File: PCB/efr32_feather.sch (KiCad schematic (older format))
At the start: 38 parts, among them J1 Feather_1, J2 USB, J3 Battery, J4 Feather_2, J5 DEBUG, Q1 DMG2301L, SW1 RESET, U1 TPD2EUSB30, U2 AP2112K-3.3, U3 CP2102N-A01-GQFN24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

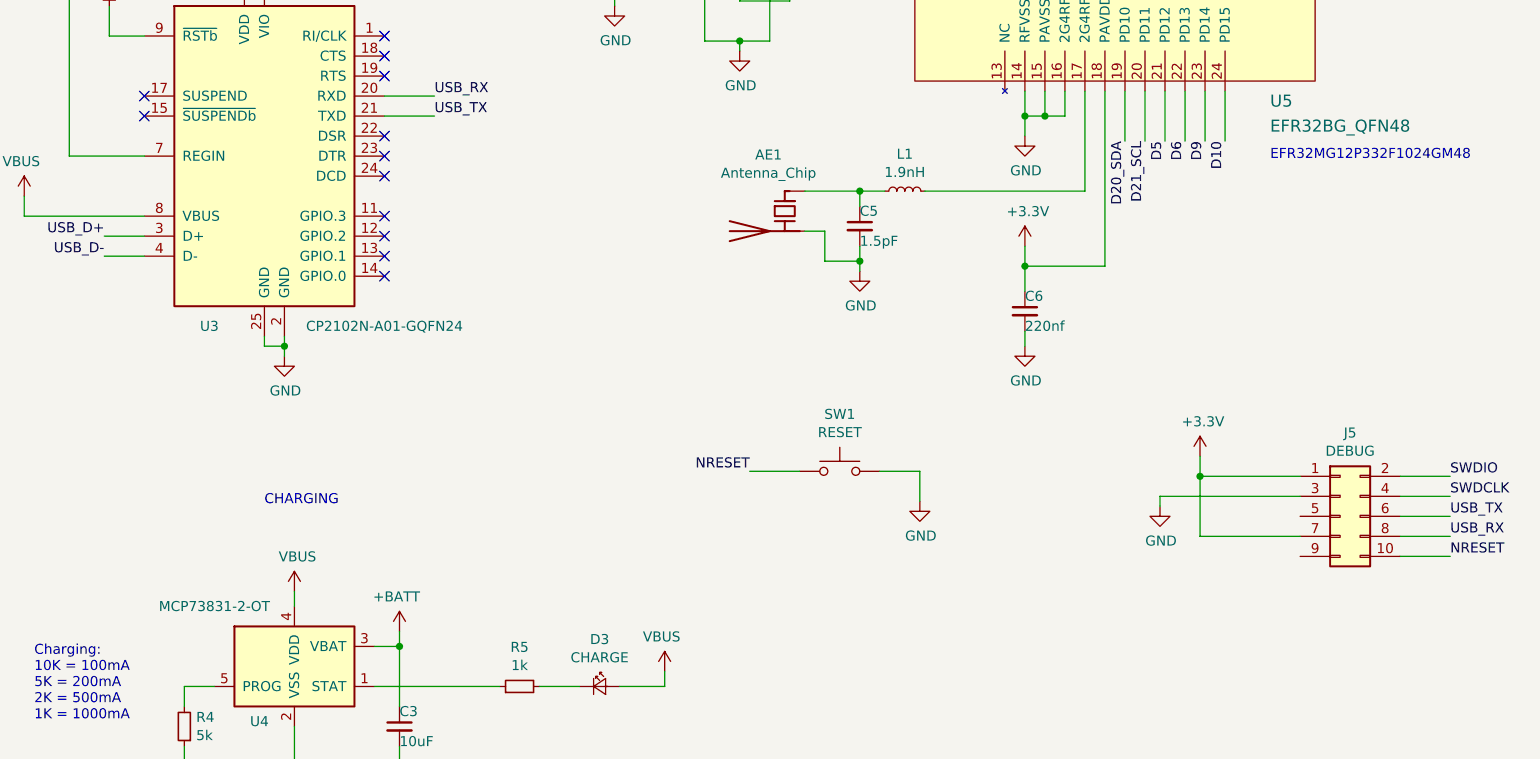
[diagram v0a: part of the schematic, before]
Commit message: Change debug connector
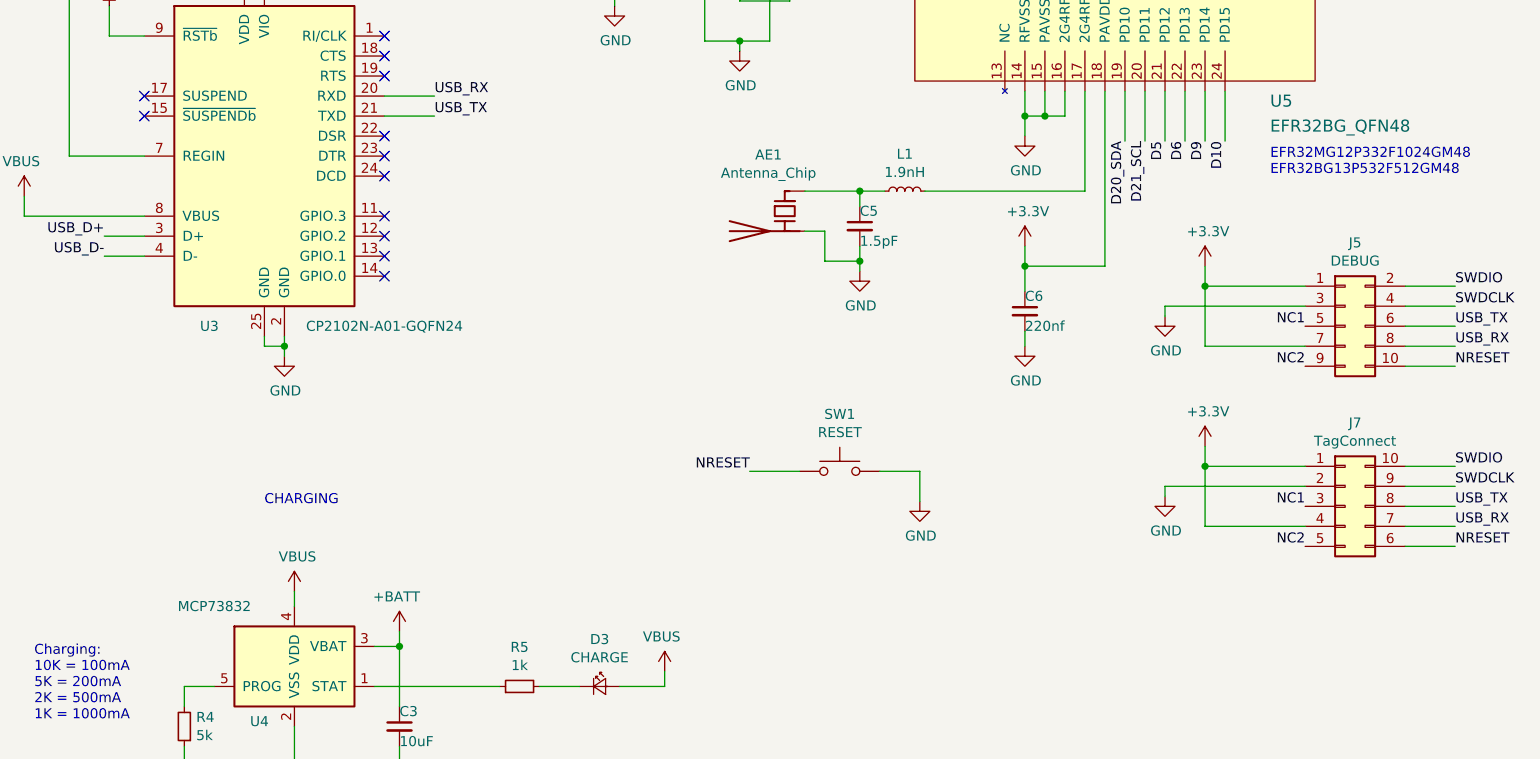
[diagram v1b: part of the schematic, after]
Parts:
- added J7: TagConnect, Connector:Tag-Connect_TC2050-IDC-NL_2x05_P1.27mm_Vertical, symbol Connector_Generic:Conn_02x05_Counter_Clockwise
- J5: footprint Connector_PinHeader_1.00mm:PinHeader_2x05_P1.00mm_Vertical_SMD -> Connector_PinHeader_1.27mm:PinHeader_2x05_P1.27mm_Vertical_SMD
- U4: value MCP73831-2-OT -> MCP73832
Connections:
- net +3V3: now also J7.1 (Pin_1), J7.4 (Pin_4)
- net GND: now also J7.2 (Pin_2)
- net NRESET: now also J7.6 (Pin_6)
- net SWDCLK: now also J7.9 (Pin_9)
- net SWDIO: now also J7.10 (Pin_10)
- net USB_RX: now also J7.7 (Pin_7)
- net USB_TX: now also J7.8 (Pin_8)
- net NC1: now reaches J5.5 (Pin_5)
- net NC1: now also J7.3 (Pin_3)
- net NC2: now reaches J5.9 (Pin_9)
- net NC2: now also J7.5 (Pin_5)
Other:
- note added: "EFR32MG12P332F1024GM48\nEFR32BG13P532F512GM48"
- note removed: "EFR32MG12P332F1024GM48"
- moved on the sheet: J5
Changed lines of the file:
@@
 Sheet 1 1
 Title "EFR32 Feather"
-Date "2019-06-07"
-Rev "0.2"
+Date "2019-06-20"
+Rev "0.3"
 Comp ""
 Comment1 ""
@@
 	10875 2600 10875 2525
 NoConn ~ 9450 1900
-Text Notes 9775 4350 0    50   ~ 0
-EFR32MG12P332F1024GM48
 $Comp
 L power:+3.3V #PWR028
@@
 P 4900 6875
 F 0 "U4" H 4725 6600 50  0000 C CNN
-F 1 "MCP73831-2-OT" H 4500 7175 50  0000 C CNN
+F 1 "MCP73832" H 4500 7175 50  0000 C CNN
 F 2 "Package_TO_SOT_SMD:SOT-23-5" H 4950 6625 50  0001 L CIN
 F 3 "http://ww1.microchip.com/downloads/en/DeviceDoc/20001984g.pdf" H 4750 6825 50  0001 C CNN
@@
 	1    0    0    -1
 $EndComp
-Wire Wire Line
-	6125 6975 6325 6975
 $Comp
 L power:VBUS #PWR022
@@
 L Connector_Generic:Conn_02x05_Odd_Even J5
 U 1 1 5D2953F6
-P 10125 6125
-F 0 "J5" H 10175 6542 50  0000 C CNN
-F 1 "DEBUG" H 10175 6451 50  0000 C CNN
-F 2 "Connector_PinHeader_1.00mm:PinHeader_2x05_P1.00mm_Vertical_SMD" H 10125 6125 50  0001 C CNN
-F 3 "~" H 10125 6125 50  0001 C CNN
-	1    10125 6125
-	1    0    0    -1
-$EndComp
-Wire Wire Line
-	10425 6025 10675 6025
-Text Label 10675 6025 0    50   ~ 0
+P 10150 5175
+F 0 "J5" H 10200 5592 50  0000 C CNN
+F 1 "DEBUG" H 10200 5501 50  0000 C CNN
+F 2 "Connector_PinHeader_1.27mm:PinHeader_2x05_P1.27mm_Vertical_SMD" H 10150 5175 50  0001 C CNN
+F 3 "~" H 10150 5175 50  0001 C CNN
+	1    10150 5175
+	1    0    0    -1
+$EndComp
+Wire Wire Line
+	10450 5075 10700 5075
+Text Label 10700 5075 0    50   ~ 0
 SWDCLK
 Wire Wire Line
-	10425 5925 10675 5925
-Text Label 10675 5925 0    50   ~ 0
+	10450 4975 10700 4975
+Text Label 10700 4975 0    50   ~ 0
 SWDIO
 Wire Wire Line
@@
 D13
 Wire Wire Line
-	10425 6125 10675 6125
-Wire Wire Line
-	10425 6225 10675 6225
-Wire Wire Line
-	10425 6325 10675 6325
-Text Label 10675 6325 0    50   ~ 0
+	10450 5175 10700 5175
+Wire Wire Line
+	10450 5275 10700 5275
+Wire Wire Line
+	10450 5375 10700 5375
+Text Label 10700 5375 0    50   ~ 0
 NRESET
 $Comp
 L power:+3.3V #PWR032
 U 1 1 5D2BA86F
-P 9425 5825
-F 0 "#PWR032" H 9425 5675 50  0001 C CNN
-F 1 "+3.3V" H 9440 5998 50  0000 C CNN
-F 2 "" H 9425 5825 50  0001 C CNN
-F 3 "" H 9425 5825 50  0001 C CNN
-	1    9425 5825
-	1    0    0    -1
-$EndComp
-Wire Wire Line
-	9425 5825 9425 5925
-Wire Wire Line
-	9425 5925 9925 5925
-Wire Wire Line
-	9925 6225 9425 6225
-Wire Wire Line
-	9425 6225 9425 5925
-Connection ~ 9425 5925
+P 9450 4875
+F 0 "#PWR032" H 9450 4725 50  0001 C CNN
+F 1 "+3.3V" H 9465 5048 50  0000 C CNN
+F 2 "" H 9450 4875 50  0001 C CNN
+F 3 "" H 9450 4875 50  0001 C CNN
+	1    9450 4875
+	1    0    0    -1
+$EndComp
+Wire Wire Line
+	9450 4875 9450 4975
+Wire Wire Line
+	9450 4975 9950 4975
+Wire Wire Line
+	9950 5275 9450 5275
+Wire Wire Line
+	9450 5275 9450 4975
+Connection ~ 9450 4975
 $Comp
 L power:GND #PWR030
 U 1 1 5D2CC75F
-P 9225 6075
-F 0 "#PWR030" H 9225 5825 50  0001 C CNN
-F 1 "GND" H 9230 5902 50  0000 C CNN
-F 2 "" H 9225 6075 50  0001 C CNN
-F 3 "" H 9225 6075 50  0001 C CNN
-	1    9225 6075
-	1    0    0    -1
-$EndComp
-Wire Wire Line
-	9925 6025 9225 6025
-Wire Wire Line
-	9225 6025 9225 6075
+P 9250 5125
+F 0 "#PWR030" H 9250 4875 50  0001 C CNN
+F 1 "GND" H 9255 4952 50  0000 C CNN
+F 2 "" H 9250 5125 50  0001 C CNN
+F 3 "" H 9250 5125 50  0001 C CNN
+	1    9250 5125
+	1    0    0    -1
+$EndComp
+Wire Wire Line
+	9950 5075 9250 5075
+Wire Wire Line
+	9250 5075 9250 5125
 Wire Wire Line
 	8750 4000 8750 4125
@@
 	1    0    0    -1
 $EndComp
-Text Label 10675 6225 0    50   ~ 0
+Text Label 10700 5275 0    50   ~ 0
 USB_RX
-Text Label 10675 6125 0    50   ~ 0
+Text Label 10700 5175 0    50   ~ 0
 USB_TX
 Text Notes 4750 6075 0    50   ~ 0
@@
 Text Notes 1600 3375 0    50   ~ 0
 ESD PROTECTION
+Text Notes 9775 4425 0    50   ~ 0
+EFR32MG12P332F1024GM48\nEFR32BG13P532F512GM48
+Wire Wire Line
+	10450 5975 10700 5975
+Text Label 10700 5975 0    50   ~ 0
+SWDCLK
+Wire Wire Line
+	10450 5875 10700 5875
+Text Label 10700 5875 0    50   ~ 0
+SWDIO
+Wire Wire Line
+	10450 6075 10700 6075
+Wire Wire Line
+	10450 6175 10700 6175
+Wire Wire Line
+	10450 6275 10700 6275
+Text Label 10700 6275 0    50   ~ 0
+NRESET
+$Comp
+L power:+3.3V #PWR0103
+U 1 1 5D147AC9
+P 9450 5775
+F 0 "#PWR0103" H 9450 5625 50  0001 C CNN
+F 1 "+3.3V" H 9465 5948 50  0000 C CNN
+F 2 "" H 9450 5775 50  0001 C CNN
+F 3 "" H 9450 5775 50  0001 C CNN
+	1    9450 5775
+	1    0    0    -1
+$EndComp
+Wire Wire Line
+	9450 5775 9450 5875
+Wire Wire Line
+	9450 5875 9950 5875
+Wire Wire Line
+	9950 6175 9450 6175
+Wire Wire Line
+	9450 6175 9450 5875
+Connection ~ 9450 5875
+$Comp
+L power:GND #PWR0104
+U 1 1 5D147AD8
+P 9250 6025
+F 0 "#PWR0104" H 9250 5775 50  0001 C CNN
+F 1 "GND" H 9255 5852 50  0000 C CNN
+F 2 "" H 9250 6025 50  0001 C CNN
+F 3 "" H 9250 6025 50  0001 C CNN
+	1    9250 6025
+	1    0    0    -1
+$EndComp
+Wire Wire Line
+	9950 5975 9250 5975
+Wire Wire Line
+	9250 5975 9250 6025
+Text Label 10700 6175 0    50   ~ 0
+USB_RX
+Text Label 10700 6075 0    50   ~ 0
+USB_TX
+$Comp
+L Connector_Generic:Conn_02x05_Counter_Clockwise J7
+U 1 1 5D160015
+P 10150 6075
+F 0 "J7" H 10200 6492 50  0000 C CNN
+F 1 "TagConnect" H 10200 6401 50  0000 C CNN
+F 2 "Connector:Tag-Connect_TC2050-IDC-NL_2x05_P1.27mm_Vertical" H 10150 6075 50  0001 C CNN
+F 3 "~" H 10150 6075 50  0001 C CNN
+	1    10150 6075
+	1    0    0    -1
+$EndComp
+Text Label 9950 6075 2    50   ~ 0
+NC1
+Text Label 9950 6275 2    50   ~ 0
+NC2
+Text Label 9950 5175 2    50   ~ 0
+NC1
+Text Label 9950 5375 2    50   ~ 0
+NC2
+Wire Wire Line
+	6125 6975 6325 6975
 $EndSCHEMATC
